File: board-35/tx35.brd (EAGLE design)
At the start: 100 x 80 mm, 23 parts, among them J1 SWD_SHROUD, Q1 MOSFET-NCHANNEL2N7002PW, X1 SMA-142-0711-821/826

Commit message: almost done 35mhz tranasmitter
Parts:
- added C13: (no value), passives-7351:C0805-N
- added JP1: (no value), Mine:1X02
- added JP2: (no value), SparkFun-Connectors:1X06
- added R4: 10k, passives-7351:R0603-N
- IC1: value STM32F0-32 -> STM32F030K6
- moved J1 20.4 mm to (13.7, 6.99)
- moved C6 3.69 mm to (32.1, 5.21), turned to 90 degrees
- moved C4 3.01 mm to (18.9, 17.0), turned to 90 degrees
- moved X1 1.82 mm to (46.5, 11.0)
- moved L1 1.52 mm to (32.8, 14.0)
- moved C12 1.45 mm to (40.4, 12.8)
- moved C7 1.40 mm to (30.5, 5.21), turned to 90 degrees
- moved R2 1.02 mm to (21.3, 17.8)
- moved C10 0.97 mm to (37.8, 8.51)
- moved C8 0.97 mm to (34.7, 8.51)
- moved C9 0.97 mm to (37.2, 11.0)
- moved Q1 0.97 mm to (32.1, 8.51)
- moved C11 0.97 mm to (41.0, 8.51)
- moved L2 0.97 mm to (34.0, 11.0)
- moved L3 0.97 mm to (40.4, 11.0)
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- renumbered U$1 to IC1
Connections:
- new net N$12: IC1.19, JP2.5
- new net N$13: IC1.31, JP1.1, R4.1
- new net N$7: C13.1, JP2.2, L1.2
- new net N$9: IC1.20, JP2.4
- net +3V3: now also JP1.2, JP2.3
- net GND: now also C13.2, JP2.1, R4.2
- net N$5: now also JP2.6
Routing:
- net GND: track 10.3 -> 48.9 mm, vias 0 -> 20
- net NRST: track 45.2 -> 15.3 mm
- net +3V3: track 75.0 -> 52.6 mm
- net SWDCLK: track 7.05 -> 23.2 mm, vias 0 -> 2
- net N$13: track 0.00 -> 16.0 mm, vias 0 -> 3
- net SWDIO: track 9.42 -> 20.1 mm, vias 0 -> 2
- net N$9: track 0.00 -> 10.1 mm, vias 0 -> 1
- net N$12: track 0.00 -> 10.0 mm
- net N$7: track 0.00 -> 8.05 mm
- net N$6: track 10.1 -> 6.77 mm
- net N$5: track 7.03 -> 9.81 mm, vias 0 -> 1
- net N$4: track 4.38 -> 3.26 mm
- net N$8: track 5.97 -> 5.16 mm
- net MCO: track 2.76 -> 2.03 mm
- added copper zone on layer 16, net GND
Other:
- board size 100 x 80 mm -> 38.1 x 15.6 mm
- board text added: "3.3V"
- board text added: "BOOT"
- board text added: "EN"
- board text added: "GND"
- board text added: "HF Transmitter"
- board text added: "Jan 2016"
- board text added: "MOD_IN"
- board text added: "Matt Brejza"
- board text added: "SWD"
- board text added: "UART_RX"
- board text added: "V_PA"

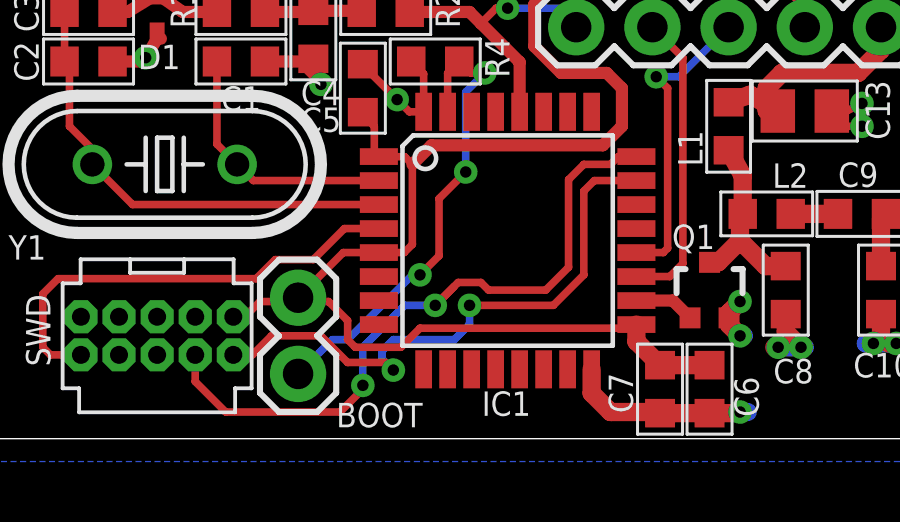
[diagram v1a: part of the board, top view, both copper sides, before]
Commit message: adding some mire testpads
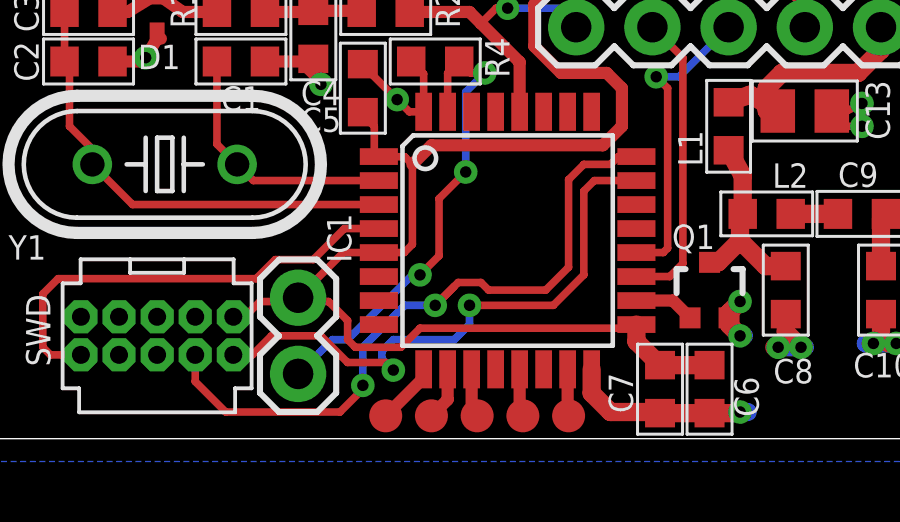
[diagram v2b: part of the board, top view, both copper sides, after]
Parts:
- added TP1, TP2, TP3, TP5, TP6: PTR1TP11R, testpad:TP11R
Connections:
- new net N$14: IC1.9, TP2.TP
- new net N$15: IC1.15, TP1.TP
- new net N$16: IC1.13, TP3.TP
- new net N$18: IC1.11, TP5.TP
- new net N$19: IC1.10, TP6.TP
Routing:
- net N$14: track 0.00 -> 2.07 mm
- net N$19: track 0.00 -> 1.77 mm
- net N$18: track 0.00 -> 1.63 mm
- net N$16: track 0.00 -> 1.59 mm
- net N$15: track 0.00 -> 1.56 mm
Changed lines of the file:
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@@
 <board>
 <plain>
-<text x="19.685" y="3.937" size="0.8128" layer="21" font="vector" ratio="14">BOOT</text>
+<text x="20.447" y="8.636" size="0.8128" layer="22" font="vector" ratio="14" rot="MR270">BOOT</text>
 <text x="10.16" y="5.969" size="0.8128" layer="21" font="vector" ratio="14" rot="R90">SWD</text>
 <circle x="40.64" y="15.621" radius="0.127" width="0.4064" layer="21"/>
@@
 <elements>
 <element name="IC1" library="Mine" package="TQFP32-08" value="STM32F030K6" x="25.4" y="10.16" smashed="yes">
-<attribute name="NAME" x="24.5364" y="4.318" size="0.8128" layer="25" font="vector" ratio="14"/>
+<attribute name="NAME" x="20.193" y="9.4234" size="0.8128" layer="25" font="vector" ratio="14" rot="R90"/>
 </element>
 <element name="Y1" library="SparkFun-FreqCtrl" package="HC49U-V" value="" x="13.97" y="12.7" smashed="yes">
@@
 <element name="C13" library="passives-7351" package="C0805-N" value="" x="35.306" y="14.478" smashed="yes">
 <attribute name="NAME" x="38.144125" y="13.51828125" size="0.8128" layer="25" font="vector" ratio="14" rot="R90"/>
+</element>
+<element name="TP1" library="testpad" package="TP11R" value="PTR1TP11R" x="27.432" y="4.318" smashed="yes">
+<attribute name="TP_SIGNAL_NAME" value="" x="27.432" y="2.413" size="1" layer="37"/>
+</element>
+<element name="TP3" library="testpad" package="TP11R" value="PTR1TP11R" x="25.908" y="4.318" smashed="yes">
+<attribute name="TP_SIGNAL_NAME" value="" x="25.908" y="2.413" size="1" layer="37"/>
+</element>
+<element name="TP5" library="testpad" package="TP11R" value="PTR1TP11R" x="24.384" y="4.318" smashed="yes">
+<attribute name="TP_SIGNAL_NAME" value="" x="24.384" y="2.413" size="1" layer="37"/>
+</element>
+<element name="TP6" library="testpad" package="TP11R" value="PTR1TP11R" x="22.86" y="4.318" smashed="yes">
+<attribute name="TP_SIGNAL_NAME" value="" x="22.86" y="2.413" size="1" layer="37"/>
+</element>
+<element name="TP2" library="testpad" package="TP11R" value="PTR1TP11R" x="21.336" y="4.318" smashed="yes">
+<attribute name="TP_SIGNAL_NAME" value="" x="21.336" y="2.413" size="1" layer="37"/>
 </element>
 </elements>
@@
 <wire x1="24.168" y1="15.748" x2="23.787" y2="16.129" width="0.254" layer="1"/>
 </signal>
+<signal name="N$15">
+<contactref element="IC1" pad="15"/>
+<contactref element="TP1" pad="TP"/>
+<wire x1="27.4" y1="5.8674" x2="27.4" y2="4.35" width="0.4064" layer="1"/>
+<wire x1="27.4" y1="4.35" x2="27.432" y2="4.318" width="0.4064" layer="1"/>
+</signal>
+<signal name="N$16">
+<contactref element="IC1" pad="13"/>
+<contactref element="TP3" pad="TP"/>
+<wire x1="25.8" y1="5.8674" x2="25.8" y2="4.426" width="0.4064" layer="1"/>
+<wire x1="25.8" y1="4.426" x2="25.908" y2="4.318" width="0.4064" layer="1"/>
+</signal>
+<signal name="N$18">
+<contactref element="IC1" pad="11"/>
+<contactref element="TP5" pad="TP"/>
+<wire x1="24.2" y1="5.8674" x2="24.2" y2="4.502" width="0.4064" layer="1"/>
+<wire x1="24.2" y1="4.502" x2="24.384" y2="4.318" width="0.4064" layer="1"/>
+</signal>
+<signal name="N$19">
+<contactref element="IC1" pad="10"/>
+<contactref element="TP6" pad="TP"/>
+<wire x1="23.4" y1="5.8674" x2="23.4" y2="4.858" width="0.4064" layer="1"/>
+<wire x1="23.4" y1="4.858" x2="22.86" y2="4.318" width="0.4064" layer="1"/>
+</signal>
+<signal name="N$14">
+<contactref element="IC1" pad="9"/>
+<contactref element="TP2" pad="TP"/>
+<wire x1="22.6" y1="5.8674" x2="22.6" y2="5.582" width="0.4064" layer="1"/>
+<wire x1="22.6" y1="5.582" x2="21.336" y2="4.318" width="0.4064" layer="1"/>
+</signal>
 </signals>
